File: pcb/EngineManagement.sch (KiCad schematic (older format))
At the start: 82 parts, among them K1 SwitchedPower, K2 RS485, K5 FuelCool, K6 AltBatt, K7 FlyOil, P1 Buttons, P10 VP ButtonPlug, P2 CONN_1, P3 CONN_1, P4 CONN_1, P5 LCD, P6 J1939, P7 RelayBoard, P8 VP EnginePlug, P9 VP MultiLinkPlug, Q1 2N2907, U1 LM7808CT, U2 DPDTRelay, U3 ArdinoMinPro, U4 RS485, U5 MCP2515Shield, U6 MCP23008, U7 LM7805CT, U8 8WayRelayBoard

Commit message: Before using edge triggers for onoff
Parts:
- removed R14: 10K, Resistors_SMD:R_0805_HandSoldering, symbol R
- added D?: 1N5819, Resistors_ThroughHole:Resistor_Horizontal_RM7mm, symbol DIODE
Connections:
- net labels added: MOSI
- net labels removed: 5v150mA, MISI
- wire segments 345 -> 343
- no-connect marks 23 -> 27
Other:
- note added: "Prevent backpowering \non startup"
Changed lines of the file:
@@
 Text GLabel 13950 8250 0    60   Output ~ 0
 RX
-Text GLabel 13950 8450 0    60   Input ~ 0
-5VSwitched
 $Comp
 L GND #PWR010
@@
 Text GLabel 8200 8600 2    60   Output ~ 0
 SCK
-Text GLabel 8200 8700 2    60   Output ~ 0
+Text GLabel 8200 8700 2    60   Input ~ 0
 MISO
-Text GLabel 8200 8800 2    60   Input ~ 0
-MISI
-Text GLabel 6000 8200 0    60   Input ~ 0
+Text GLabel 8200 8800 2    60   Output ~ 0
+MOSI
+Text GLabel 6150 6800 0    60   Input ~ 0
 CANINT
 Text GLabel 12100 9000 0    60   Input ~ 0
 SCK
-Text GLabel 12100 9200 0    60   Input ~ 0
+Text GLabel 12100 9200 0    60   Output ~ 0
 MISO
-Text GLabel 12100 9100 0    60   Output ~ 0
-MISI
-Text GLabel 12100 8900 0    60   Output ~ 0
+Text GLabel 12100 9100 0    60   Input ~ 0
+MOSI
+Text GLabel 6750 6750 0    60   Output ~ 0
 CANINT
 $Comp
@@
 	1    0    0    -1
 $EndComp
-Text GLabel 13100 8550 0    60   Input ~ 0
+Text GLabel 12850 7500 0    60   Input ~ 0
 5VSwitched
 Text Notes 12800 9650 0    60   ~ 0
@@
 	-1   0    0    1
 $EndComp
-Text GLabel 8300 8100 2    60   Output ~ 0
-5v150mA
 Text GLabel 4150 9250 0    60   Input ~ 0
 5V1A
@@
 $EndComp
 Text GLabel 7850 9800 0    60   Input ~ 0
-5v150mA
-$Comp
-L R R14
-U 1 1 6112FB8E
-P 12700 8100
-F 0 "R14" V 12780 8100 40  0000 C CNN
-F 1 "10K" V 12707 8101 40  0000 C CNN
-F 2 "Resistors_SMD:R_0805_HandSoldering" V 12630 8100 30  0001 C CNN
-F 3 "" H 12700 8100 30  0000 C CNN
-	1    12700 8100
-	-1   0    0    1
-$EndComp
+5VSwitched
 Text GLabel 12200 7700 0    60   Input ~ 0
-5v150mA
+5VSwitched
 Wire Wire Line
 	3900 1950 3900 1750
@@
 	5500 10150 5100 10150
 Wire Wire Line
-	5500 8600 5500 10150
-Wire Wire Line
-	5500 8600 6300 8600
+	5500 8200 5500 10150
 Wire Wire Line
 	6300 8700 5600 8700
@@
 	14050 8350 13950 8350
 Wire Wire Line
-	14050 8450 13950 8450
+	13050 8450 14050 8450
 Wire Notes Line
 	1500 4050 13250 4050
@@
 	15300 9250 15600 9250
 Wire Wire Line
-	12100 8900 12750 8900
-Wire Wire Line
-	13100 8550 13350 8550
+	13050 8550 13350 8550
 Wire Wire Line
 	13350 8550 13350 8650
@@
 Connection ~ 5300 8500
 Wire Wire Line
-	6000 8200 6300 8200
+	5500 8200 6300 8200
 Wire Wire Line
 	12550 9600 12550 9400
@@
 Connection ~ 5800 9900
 Wire Wire Line
-	8300 8100 7800 8100
-Wire Wire Line
 	4150 9250 5400 9250
 Wire Wire Line
@@
 Connection ~ 8150 9800
 Wire Wire Line
-	12200 7700 12700 7700
-Wire Wire Line
-	12700 7700 12700 7850
-Wire Wire Line
-	12700 8350 12700 8900
-Connection ~ 12700 8900
+	12200 7700 12300 7700
 $Comp
 L R R13
@@
 Wire Wire Line
 	12300 7700 12300 7850
-Connection ~ 12300 7700
 Wire Wire Line
 	12100 9200 12750 9200
@@
 	14150 2550 14250 2550
 Connection ~ 14150 2350
+NoConn ~ 7800 8100
+NoConn ~ 2700 3400
+$Comp
+L DIODE D?
+U 1 1 611CBF49
+P 13050 7950
+F 0 "D?" H 13050 8050 40  0000 C CNN
+F 1 "1N5819" H 13050 7850 40  0000 C CNN
+F 2 "Resistors_ThroughHole:Resistor_Horizontal_RM7mm" H 13050 7950 60  0001 C CNN
+F 3 "" H 13050 7950 60  0000 C CNN
+	1    13050 7950
+	0    1    1    0
+$EndComp
+Wire Wire Line
+	12850 7500 13050 7500
+Wire Wire Line
+	13050 7500 13050 7750
+Wire Wire Line
+	13050 8150 13050 8550
+Connection ~ 13050 8450
+Text Notes 13100 7800 0    39   ~ 0
+Prevent backpowering \non startup
+NoConn ~ 12750 8900
+NoConn ~ 6300 8600
 $EndSCHEMATC

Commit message: VP Tacho has blown Can drivers on custom ASIC, plan aborted
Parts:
- removed R13: 10K, Resistors_SMD:R_0805_HandSoldering, symbol R
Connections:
- net labels removed: CANINT
- no-connect marks 27 -> 25
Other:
- note added: "ProMini only has interrupts on pins 2 and 3\nThere is a 10K pullup on the reset on board."
- note removed: "ProMini only has interrupts on pins 2 and 3"
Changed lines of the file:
@@
 Text GLabel 8200 8800 2    60   Output ~ 0
 MOSI
-Text GLabel 6150 6800 0    60   Input ~ 0
-CANINT
 Text GLabel 12100 9000 0    60   Input ~ 0
 SCK
@@
 Text GLabel 12100 9100 0    60   Input ~ 0
 MOSI
-Text GLabel 6750 6750 0    60   Output ~ 0
-CANINT
 $Comp
 L GND #PWR011
@@
 CANCS
 Text Notes 5300 7350 0    60   ~ 0
-ProMini only has interrupts on pins 2 and 3
+ProMini only has interrupts on pins 2 and 3\nThere is a 10K pullup on the reset on board.
 Text GLabel 5150 10650 0    60   Output ~ 0
 StopBtn
@@
 NoConn ~ 7250 7400
 NoConn ~ 7350 7400
-NoConn ~ 6300 8000
-NoConn ~ 7800 8000
 Text GLabel 10150 7200 1    60   Input ~ 0
 Excitation
@@
 Text GLabel 7850 9800 0    60   Input ~ 0
 5VSwitched
-Text GLabel 12200 7700 0    60   Input ~ 0
-5VSwitched
 Wire Wire Line
 	3900 1950 3900 1750
@@
 	8150 9850 8150 9800
 Connection ~ 8150 9800
-Wire Wire Line
-	12200 7700 12300 7700
-$Comp
-L R R13
-U 1 1 6113183B
-P 12300 8100
-F 0 "R13" V 12380 8100 40  0000 C CNN
-F 1 "10K" V 12307 8101 40  0000 C CNN
-F 2 "Resistors_SMD:R_0805_HandSoldering" V 12230 8100 30  0001 C CNN
-F 3 "" H 12300 8100 30  0000 C CNN
-	1    12300 8100
-	-1   0    0    1
-$EndComp
-Wire Wire Line
-	12300 8350 12300 9300
-Connection ~ 12300 9300
-Wire Wire Line
-	12300 7700 12300 7850
 Wire Wire Line
 	12100 9200 12750 9200
@@
 	14150 2550 14250 2550
 Connection ~ 14150 2350
-NoConn ~ 7800 8100
 NoConn ~ 2700 3400
 $Comp
@@
 Prevent backpowering \non startup
 NoConn ~ 12750 8900
-NoConn ~ 6300 8600
+NoConn ~ 7800 8000
+NoConn ~ 7800 8100
+Wire Wire Line
+	6300 8000 6250 8000
+Wire Wire Line
+	6250 8000 6250 8600
+Wire Wire Line
+	6250 8600 6300 8600
 $EndSCHEMATC

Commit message: Redesigned to not use VP J1939 instruments
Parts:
- removed C11: 10nF, Capacitors_SMD:C_0805_HandSoldering, symbol C
- removed D10, D8: 10A 600V, symbol DIODE
- removed D2: SMBJ30CA-TR TSV, Diodes_SMD:DO-214AB_Handsoldering, symbol DIODE
- removed D4, D?: 1N5819, Resistors_ThroughHole:Resistor_Horizontal_RM7mm, symbol DIODE
- removed D7: 5A 600V, symbol DIODE
- removed D9: 1A 40V, symbol DIODE
- removed F1: FUSE 5A, Fuse_Holders_and_Fuses:BladeFuse-Mini, symbol FUSE
- removed F2: FUSE 40A, Fuse_Holders_and_Fuses:BladeFuse-Mini, symbol FUSE
- removed F?: 6A Breaker, symbol FUSE
- removed F? (x2): 6A breaker, symbol FUSE
- removed K2: RS485, Connect:bornier3, symbol CONN_3
- removed Max5W1: R, symbol R
- removed P1: Buttons, Connect:bornier6, symbol CONN_6
- removed P10: VP ButtonPlug, symbol CONN_6
- removed P2, P3, P4: CONN_1, Divers:M5Bolt, symbol CONN_1
- removed P5: LCD, Pin_Headers:Pin_Header_Straight_1x04, symbol CONN_4
- removed P6: J1939, Connect:bornier4, symbol CONN_4
- removed P7: RelayBoard, Pin_Headers:Pin_Header_Straight_1x10, symbol CONN_10
- removed P8: VP EnginePlug, symbol CONN_8
- removed P9: VP MultiLinkPlug, symbol CONN_6
- removed Q1: 2N2907, TO_SOT_Packages_THT:TO-92_Molded_Wide_Oval, symbol PNP
- removed R12, R19: 10K, Resistors_SMD:R_0805_HandSoldering, symbol R
- removed R29, R31: 1M, Resistors_SMD:R_0805_HandSoldering, symbol R
- removed R32: 470K, Resistors_SMD:R_0805_HandSoldering, symbol R
- removed R9: 10R, Resistors_SMD:R_0805_HandSoldering, symbol R
- removed RL1: EnginePower, Divers:AutomotiveRelay35A, symbol AutomotiveRelay
- removed RL2: EngineStart, Divers:AutomotiveRelay35A, symbol AutomotiveRelay
- removed RL3: EngineStop, Divers:AutomotiveRelay35A, symbol AutomotiveRelay
- removed RL4: GlowPlugs, Divers:AutomotiveRelay35A, symbol AutomotiveRelay
- removed U2: DPDTRelay, Housings_DIP:DIP-16_W7.62mm, symbol DPDTRelay
- removed U4: RS485, Divers:RS485Board, symbol RS485
- removed U6: MCP23008, Housings_DIP:DIP-18_W7.62mm, symbol MCP23008
- removed U7: LM7805CT, TO_SOT_Packages_THT:TO-220_Horizontal, symbol LM7808CT
- removed U8: 8WayRelayBoard, Housings_DIP:DIP-28_W7.62mm, symbol 8WayRelayBoard
- added C12, C13: 10nF, Capacitors_SMD:C_0805_HandSoldering, symbol C
- added TH1: 500mA Thermistor, Resistors_ThroughHole:Resistor_Horizontal_RM7mm, symbol THERMISTOR
- C6: value 1nF -> 10nF
- K1: value SwitchedPower -> Temps
- K6: value AltBatt -> FuelCoolAlt
- K7: value FlyOil -> Supply
- R1: value 2.2K -> 1M
- R10, R11, R8: value 10K -> 22K
- R2, R6, R7: value 10K -> 100K
- U1: footprint TO_SOT_Packages_THT:TO-220_Horizontal -> TO_SOT_Packages_SMD:TO-263-3Lead
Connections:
- net labels added: 12V, 5V150mA, NTC1, NTC2, NTC3
- net labels removed: 0V, 0V-SB, 5V1A, 5VSwitched, 8VSwitched, AccDimmer-W, AlternatorExcitation, Battery+, BatteryProtected+, BatterySwitched+, BatteryUnfused+, Buzzer-?, CanH-Y/W, CanL-Y/GR, CoolantSensorVP-LBN, EngineRoomFan, Excitation, ExcitationVP, FlywheelVP+-GR/SB, FlywheelVP--GR, FuelLevel-, GlowBtn, GlowPlugs, KeelController, MultiLink0V-SB, MultiLink12V-R, OilPressure, OilPressureVP-SB, OnOff-R, OnOffBtn, PowerEnable, RX, SCL, SDA, STOP-VO, Start-Y, StartBtn, StarterSolenoidT30, StopBtn, StopSolenoid, StopSolenoid-VO, TX, WindlassController
- wire segments 343 -> 110
- no-connect marks 25 -> 10
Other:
- note added: "Can board with trancever built in. \nUsing Onboard connector\n"
- note added: "Coolant Sensor\n120C == 22R\n0C = 1743R\n120C == 8*22/(1000+22)=0.17V\n80C = 8*70/1000+70)=0.52V \n50C = 8*197/1000+70)=1.3V\n8mA\n\n\n"
- note added: "Fuel Sensor\n0R == Empty\n190R == Full\nSupply 8V Use 1K, Full 1.2V empty 0v\nCurrent max 8mA, 64mW\n"
- note added: "NTC MF52-10K\n100K at 0C 5*100/(100+10)=4.5v \n25K at 5C 5*25/(25+10)=3.5v\n10K at 20C 5*10/(10+10)=2.5v\n506R at 110C 5*0.506/(0.506+10)=0.179v\n\nx =22K\n\n\n\n\n\n"
- note removed: "0R == Empty\n190R == Full\nSupply 8V Use 1K, Full 1.2V empty 0v\nCurrent max 8mA, 64mW\n"
- note removed: "120C == 22R\n0C = 1743R\n120C == 8*22/(1000+22)=0.17V\n80C = 8*70/1000+70)=0.52V \n50C = 8*197/1000+70)=1.3V\n8mA\n\n\n"
- note removed: "20A"
- note removed: "30A"
- note removed: "3A protected connector"
- note removed: "40A protected connector"
- note removed: "8A"
- note removed: "Additional engine connector"
- note removed: "Can board with trancever built in."
- note removed: "Connects to relay driver boards via ribbon cable.\nRelay Driver is opto isolated"
- note removed: "J1939 interface if we want to use the Volvo Penta tachometer."
- note removed: "LCD I2C connector (pin header)\n"
- note removed: "Manually Wired with Crimp connectors"
- note removed: "Prevent backpowering \non startup"
- note removed: "Protectets agains the higher power circuits being \ndamaged or locked on after a surge.."
- note removed: "RS485 link to NMEA2000 converter"
- note removed: "SB,BL,BL,BL\n"
- note removed: "SB,BL,BL,Y\n"
- note removed: "SB,BL,BL\n"
- note removed: "SB,BL,R\n"
- note removed: "SB,BL,W\n"
- note removed: "SB,BL,Y\n"
- note removed: "SB,SB,BL\n"
- note removed: "SB,SB,R\n"
- note removed: "SB,SB,SB,BL\n"
- note removed: "SB,SB,SB,R\n"
- note removed: "SB,SB,SB,W\n"
- note removed: "SB,SB,SB,Y\n"
- note removed: "SB,SB,W\n"
- note removed: "SB,SB,Y\n"
- note removed: "SB,Y,BL\n"
- note removed: "SB,Y,R\n"
- note removed: "SB,Y,W\n"
- note removed: "SB,Y,Y,BL\n"
- note removed: "SB,Y,Y,Y\n"
- note removed: "SB,Y,Y\n"
- note removed: "Standard Volvo Penta Plugs\nSB= Black, GR= Grey, W= White\nR= Red, BN= Brown, Y= Yellow\nP= Pink, BL= Blue, GN= Green\nOR= Orange, VO= Violet"
- note removed: "The TSV should fail closed and blow the fuse \nbreaking supply to all relays which will fail open and safe.\nThe fuse should not be > 10A, ideally < 1A as it should only be powering low power parts."
- note removed: "The cut down ARD1939 stack needs 8K program space out of \n30K available so should run on a Pro-Mini. It will only talk to the tacho,\nand is not likely to need much."
- note removed: "The oil pressure switch is normall closed at rest so use switched 5V"
- note removed: "To Push buttons via 6 pin deutz"
- note removed: "To engine loom connector, 8 pin"
- note removed: "Using non micro 5v as we may need to \npull up more agressively due to the \nlength of the wires"
- note removed: "Volvo Penta Soft buttons"
- note removed: "Wire codes. SB,BL,Y,R,W\nCode always starts with SB. \nSecond code marks the connector, \n3rd and 4th code marks the wire.\nAll these wires will probably be in a single conduit."
- moved on the sheet: C1, C10, C4, C5, C6, C7, C8, D1, D5, D6, K5, K6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

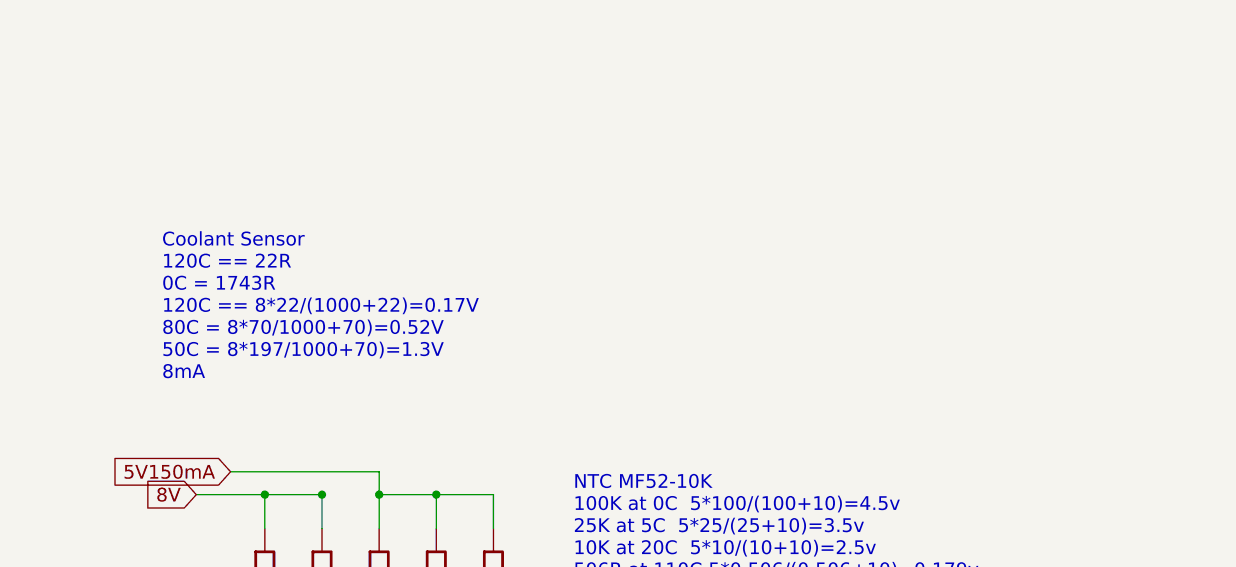
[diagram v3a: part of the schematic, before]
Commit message: NTC sensors working correctly
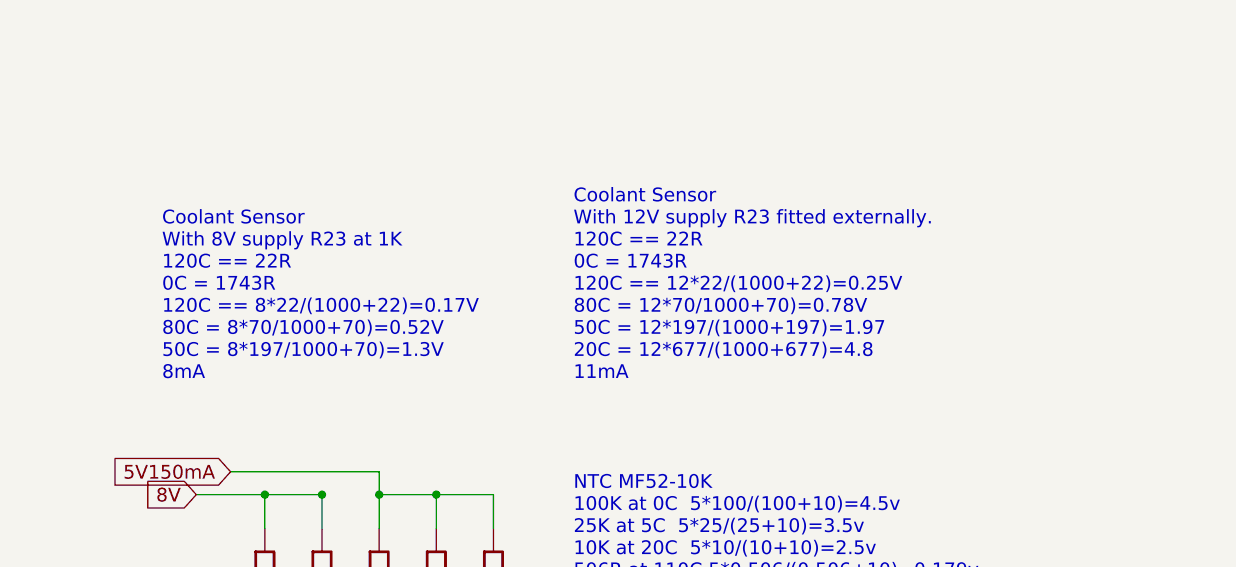
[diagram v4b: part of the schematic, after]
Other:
- note added: "Coolant Sensor\nWith 12V supply R23 fitted externally.\n120C == 22R\n0C = 1743R\n120C == 12*22/(1000+22)=0.25V\n80C = 12*70/1000+70)=0.78V \n50C = 12*197/(1000+197)=1.97\n20C = 12*677/(1000+677)=4.8\n11mA\n\n\n"
- note added: "Coolant Sensor\nWith 8V supply R23 at 1K\n120C == 22R\n0C = 1743R\n120C == 8*22/(1000+22)=0.17V\n80C = 8*70/1000+70)=0.52V \n50C = 8*197/1000+70)=1.3V\n8mA\n\n\n"
- note removed: "Coolant Sensor\n120C == 22R\n0C = 1743R\n120C == 8*22/(1000+22)=0.17V\n80C = 8*70/1000+70)=0.52V \n50C = 8*197/1000+70)=1.3V\n8mA\n\n\n"
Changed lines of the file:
@@
 Fuel Sensor\n0R == Empty\n190R ==  Full\nSupply 8V Use 1K, Full 1.2V empty 0v\nCurrent  max 8mA, 64mW\n
 Text Notes 8000 3600 0    60   ~ 0
-Coolant Sensor\n120C == 22R\n0C = 1743R\n120C == 8*22/(1000+22)=0.17V\n80C = 8*70/1000+70)=0.52V \n50C = 8*197/1000+70)=1.3V\n8mA\n\n\n
+Coolant Sensor\nWith 8V supply R23 at 1K\n120C == 22R\n0C = 1743R\n120C == 8*22/(1000+22)=0.17V\n80C = 8*70/1000+70)=0.52V \n50C = 8*197/1000+70)=1.3V\n8mA\n\n\n
 $Comp
 L MCP2515Shield U5
@@
 NTC3
 $Comp
-L GND #PWR010
+L GND #PWR09
 U 1 1 612B95DA
 P 5200 6700
-F 0 "#PWR010" H 5200 6700 30  0001 C CNN
+F 0 "#PWR09" H 5200 6700 30  0001 C CNN
 F 1 "GND" H 5200 6630 30  0001 C CNN
 F 2 "" H 5200 6700 60  0001 C CNN
@@
 NTC3
 $Comp
-L GND #PWR011
+L GND #PWR010
 U 1 1 612BBFFF
 P 13150 5600
-F 0 "#PWR011" H 13150 5600 30  0001 C CNN
+F 0 "#PWR010" H 13150 5600 30  0001 C CNN
 F 1 "GND" H 13150 5530 30  0001 C CNN
 F 2 "" H 13150 5600 60  0001 C CNN
@@
 Text GLabel 12600 5700 0    60   Input ~ 0
 8V
+Text Notes 9800 3600 0    60   ~ 0
+Coolant Sensor\nWith 12V supply R23 fitted externally.\n120C == 22R\n0C = 1743R\n120C == 12*22/(1000+22)=0.25V\n80C = 12*70/1000+70)=0.78V \n50C = 12*197/(1000+197)=1.97\n20C = 12*677/(1000+677)=4.8\n11mA\n\n\n
 $EndSCHEMATC

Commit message: Added pdfs for reference
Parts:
- removed R5: 10K, Resistors_SMD:R_0805_HandSoldering, symbol R
- R10, R11, R8: value 22K -> 4.7K
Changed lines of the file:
@@
 Text Notes 1200 4550 0    60   ~ 0
 Signal at idle is 32v pkp, 415Hz, and rises \nfrom there as the engine speed picks up.\n\nAt idle the power disipated in the diodes is uW. \nAt 3KHz, 150V pkp currents in diodes a 1mA or less\nAt 415Hz 32v voltage across caps is < 20v\n
-$Comp
-L R R5
-U 1 1 61121604
-P 4850 4450
-F 0 "R5" V 4930 4450 40  0000 C CNN
-F 1 "10K" V 4857 4451 40  0000 C CNN
-F 2 "Resistors_SMD:R_0805_HandSoldering" V 4780 4450 30  0001 C CNN
-F 3 "" H 4850 4450 30  0000 C CNN
-	1    4850 4450
-	-1   0    0    1
-$EndComp
 NoConn ~ 3200 7600
 NoConn ~ 7050 4550
@@
 	7050 4950 7450 4950
 Wire Wire Line
-	8450 4550 8450 6200
-Wire Wire Line
-	7950 5050 11050 5050
+	8450 4550 8450 5050
+Wire Wire Line
+	8450 5050 8450 6200
+Wire Wire Line
+	7950 5050 8450 5050
+Wire Wire Line
+	8450 5050 11050 5050
 Connection ~ 8450 5050
 Wire Wire Line
-	8150 3900 8700 3900
-Wire Wire Line
-	8950 3900 9450 3900
+	8150 3900 8450 3900
+Wire Wire Line
+	8450 3900 8700 3900
+Wire Wire Line
+	8950 3900 9200 3900
+Wire Wire Line
+	9200 3900 9450 3900
 Wire Wire Line
 	8450 4050 8450 3900
 Wire Wire Line
-	8450 6600 8450 6850
+	8450 6600 8450 6700
+Wire Wire Line
+	8450 6700 8450 6850
 Connection ~ 8450 6700
 Wire Wire Line
@@
 	7550 4350 7050 4350
 Wire Wire Line
-	4600 1150 5650 1150
+	4600 1150 4850 1150
+Wire Wire Line
+	4850 1150 5150 1150
+Wire Wire Line
+	5150 1150 5350 1150
+Wire Wire Line
+	5350 1150 5650 1150
 Wire Wire Line
 	5350 1400 5350 1150
 Connection ~ 5350 1150
 Wire Wire Line
-	5150 1850 6750 1850
+	5150 1850 5350 1850
+Wire Wire Line
+	5350 1850 6050 1850
+Wire Wire Line
+	6050 1850 6750 1850
 Wire Wire Line
 	6750 1850 6750 1800
@@
 	5350 1850 5350 1800
 Wire Wire Line
-	6050 1450 6050 2050
+	6050 1450 6050 1850
+Wire Wire Line
+	6050 1850 6050 2050
 Connection ~ 6050 1850
 Wire Wire Line
-	6450 1150 6900 1150
+	6450 1150 6750 1150
+Wire Wire Line
+	6750 1150 6900 1150
 Wire Wire Line
 	6750 1150 6750 1400
 Wire Wire Line
-	8450 6700 9900 6700
+	8450 6700 8700 6700
+Wire Wire Line
+	8700 6700 8950 6700
+Wire Wire Line
+	8950 6700 9200 6700
+Wire Wire Line
+	9200 6700 9450 6700
+Wire Wire Line
+	9450 6700 9700 6700
+Wire Wire Line
+	9700 6700 9900 6700
 Wire Notes Line
 	800  6000 900  6000
@@
 Connection ~ 5350 1850
 Wire Wire Line
-	4850 4800 3950 4800
-Wire Wire Line
-	4400 4600 4400 4850
+	4850 4800 4400 4800
+Wire Wire Line
+	4400 4800 3950 4800
+Wire Wire Line
+	4400 4600 4400 4800
+Wire Wire Line
+	4400 4800 4400 4850
 Connection ~ 4400 4800
 Wire Wire Line
@@
 	4400 5300 4150 5300
 Wire Wire Line
-	4150 5100 4150 5350
+	4150 5100 4150 5300
+Wire Wire Line
+	4150 5300 4150 5350
 Wire Wire Line
 	4150 5100 3950 5100
@@
 	2900 5100 2700 5100
 Wire Wire Line
-	4850 4700 4850 4800
+	4850 4750 4850 4800
 Wire Wire Line
 	4400 4150 4400 4200
 Wire Wire Line
-	3900 4150 4850 4150
-Wire Wire Line
 	3900 4150 3900 4250
 Wire Wire Line
 	3900 4250 3800 4250
-Wire Wire Line
-	4850 4150 4850 4200
-Connection ~ 4400 4150
 Wire Wire Line
 	2550 7900 3200 7900
@@
 	2550 7700 3200 7700
 Connection ~ 8450 3900
-Connection ~ 4850 4750
 Wire Wire Line
 	3400 7250 3800 7250
 Wire Wire Line
-	7050 5650 10050 5650
+	7050 5650 9700 5650
+Wire Wire Line
+	9700 5650 9900 5650
+Wire Wire Line
+	9900 5650 10050 5650
 Wire Wire Line
 	7050 5550 7400 5550
@@
 P 8950 4300
 F 0 "R8" V 9030 4300 40  0000 C CNN
-F 1 "22K" V 8957 4301 40  0000 C CNN
+F 1 "4.7K" V 8957 4301 40  0000 C CNN
 F 2 "Resistors_SMD:R_0805_HandSoldering" V 8880 4300 30  0001 C CNN
 F 3 "" H 8950 4300 30  0000 C CNN
@@
 P 9200 4300
 F 0 "R10" V 9280 4300 40  0000 C CNN
-F 1 "22K" V 9207 4301 40  0000 C CNN
+F 1 "4.7K" V 9207 4301 40  0000 C CNN
 F 2 "Resistors_SMD:R_0805_HandSoldering" V 9130 4300 30  0001 C CNN
 F 3 "" H 9200 4300 30  0000 C CNN
@@
 P 9450 4300
 F 0 "R11" V 9530 4300 40  0000 C CNN
-F 1 "22K" V 9457 4301 40  0000 C CNN
+F 1 "4.7K" V 9457 4301 40  0000 C CNN
 F 2 "Resistors_SMD:R_0805_HandSoldering" V 9380 4300 30  0001 C CNN
 F 3 "" H 9450 4300 30  0000 C CNN
@@
 Connection ~ 8700 3900
 Wire Wire Line
-	8700 4550 8700 6200
-Wire Wire Line
-	8950 4550 8950 6200
-Wire Wire Line
-	9200 4550 9200 6200
+	8700 4550 8700 4950
+Wire Wire Line
+	8700 4950 8700 6200
+Wire Wire Line
+	8950 4550 8950 4850
+Wire Wire Line
+	8950 4850 8950 6200
+Wire Wire Line
+	9200 4550 9200 4750
+Wire Wire Line
+	9200 4750 9200 6200
 Wire Wire Line
 	8700 6700 8700 6600
@@
 Connection ~ 9200 6700
 Wire Wire Line
-	9450 4550 9450 6200
-Wire Wire Line
-	8950 3800 8950 4050
+	9450 4550 9450 5550
+Wire Wire Line
+	9450 5550 9450 6200
+Wire Wire Line
+	8950 3800 8950 3900
+Wire Wire Line
+	8950 3900 8950 4050
 Wire Wire Line
 	9200 3900 9200 4050
@@
 Connection ~ 9200 3900
 Wire Wire Line
-	7950 4950 11050 4950
+	7950 4950 8700 4950
+Wire Wire Line
+	8700 4950 11050 4950
 Connection ~ 8700 4950
 Wire Wire Line
-	7950 4850 11050 4850
+	7950 4850 8950 4850
+Wire Wire Line
+	8950 4850 11050 4850
 Connection ~ 8950 4850
 Wire Wire Line
-	7950 4750 11050 4750
+	7950 4750 9200 4750
+Wire Wire Line
+	9200 4750 11050 4750
 Connection ~ 9200 4750
 Wire Wire Line
-	7900 5550 10950 5550
+	7900 5550 9450 5550
+Wire Wire Line
+	9450 5550 10950 5550
 Connection ~ 9450 5550
 Wire Wire Line
@@
 $EndComp
 Wire Wire Line
-	4400 5550 5550 5550
+	4400 5550 5000 5550
+Wire Wire Line
+	5000 5550 5200 5550
+Wire Wire Line
+	5200 5550 5550 5550
 $Comp
 L R R1
@@
 $EndComp
 Wire Wire Line
-	4400 5650 5550 5650
+	4400 5650 4550 5650
+Wire Wire Line
+	4550 5650 4750 5650
+Wire Wire Line
+	4750 5650 5550 5650
 Text GLabel 10950 5650 2    60   Input ~ 0
 AlternatorB+
@@
 $EndComp
 Wire Wire Line
-	5200 6450 5200 6700
-Wire Wire Line
-	4550 6600 5200 6600
+	5200 6450 5200 6600
+Wire Wire Line
+	5200 6600 5200 6700
+Wire Wire Line
+	4550 6600 4750 6600
+Wire Wire Line
+	4750 6600 5000 6600
+Wire Wire Line
+	5000 6600 5200 6600
 Wire Wire Line
 	4550 6600 4550 6450
@@
 Text Notes 9800 3600 0    60   ~ 0
 Coolant Sensor\nWith 12V supply R23 fitted externally.\n120C == 22R\n0C = 1743R\n120C == 12*22/(1000+22)=0.25V\n80C = 12*70/1000+70)=0.78V \n50C = 12*197/(1000+197)=1.97\n20C = 12*677/(1000+677)=4.8\n11mA\n\n\n
+Wire Wire Line
+	3900 4150 4400 4150
 $EndSCHEMATC
